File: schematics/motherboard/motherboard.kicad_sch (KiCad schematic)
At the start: 2 parts, among them J1 BATTERY, U1 Raspberry_Pi_Pico

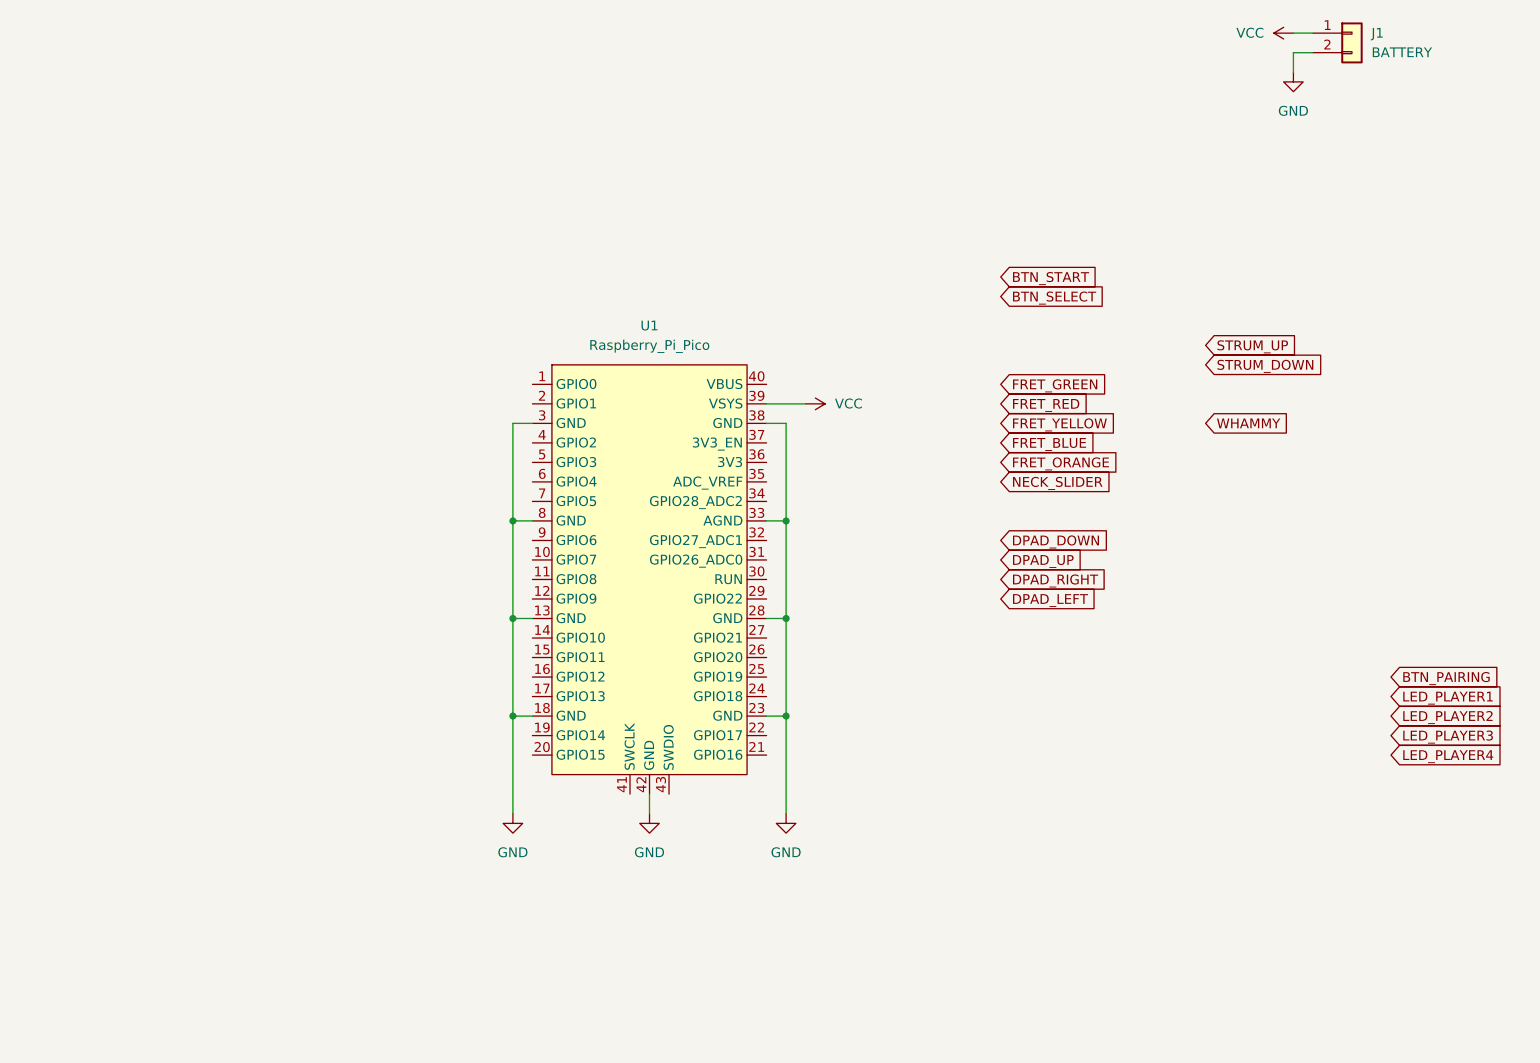
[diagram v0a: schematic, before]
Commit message: Update fret_board, motherboard and strum_bar schematics
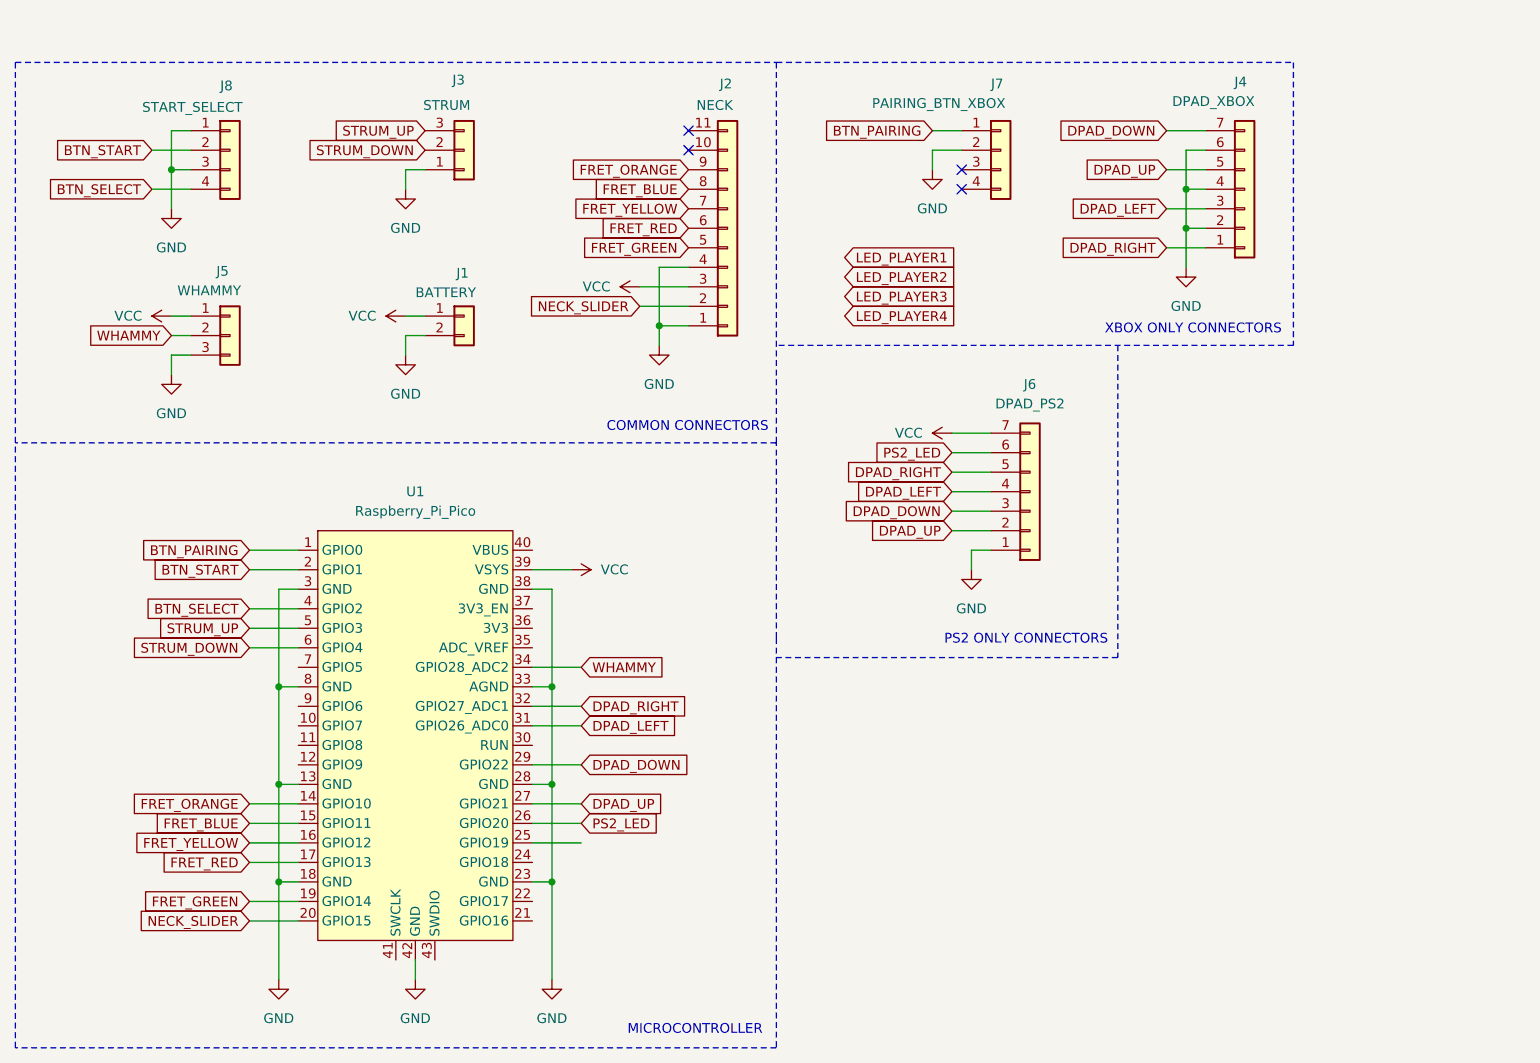
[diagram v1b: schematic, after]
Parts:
- added J2: NECK, Connector_PinHeader_2.00mm:PinHeader_1x11_P2.00mm_Vertical, symbol Connector_Generic:Conn_01x11
- added J3: STRUM, Connector_PinHeader_2.00mm:PinHeader_1x03_P2.00mm_Vertical, symbol Connector_Generic:Conn_01x03
- added J4: DPAD_XBOX, Connector_PinHeader_2.00mm:PinHeader_1x07_P2.00mm_Vertical, symbol Connector_Generic:Conn_01x07
- added J5: WHAMMY, Connector_PinHeader_2.00mm:PinHeader_1x03_P2.00mm_Vertical, symbol Connector_Generic:Conn_01x03
- added J6: DPAD_PS2, Connector_PinHeader_2.00mm:PinHeader_1x07_P2.00mm_Vertical, symbol Connector_Generic:Conn_01x07
- added J7: PAIRING_BTN_XBOX, Connector_PinHeader_2.00mm:PinHeader_1x04_P2.00mm_Vertical, symbol Connector_Generic:Conn_01x04
- added J8: START_SELECT, Connector_PinHeader_2.00mm:PinHeader_1x04_P2.00mm_Vertical, symbol Connector_Generic:Conn_01x04
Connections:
- net BTN_PAIRING: now also U1.1 (GPIO0), J7.1 (Pin_1)
- net BTN_SELECT: now also U1.4 (GPIO2), J8.4 (Pin_4)
- net BTN_START: now also U1.2 (GPIO1), J8.2 (Pin_2)
- net DPAD_DOWN: now also U1.29 (GPIO22), J4.7 (Pin_7), J6.3 (Pin_3)
- net DPAD_LEFT: now also U1.31 (GPIO26_ADC0), J4.3 (Pin_3), J6.4 (Pin_4)
- net DPAD_RIGHT: now also U1.32 (GPIO27_ADC1), J4.1 (Pin_1), J6.5 (Pin_5)
- net DPAD_UP: now also U1.27 (GPIO21), J4.5 (Pin_5), J6.2 (Pin_2)
- net FRET_BLUE: now also U1.15 (GPIO11), J2.8 (Pin_8)
- net FRET_GREEN: now also U1.19 (GPIO14), J2.5 (Pin_5)
- net FRET_ORANGE: now also U1.14 (GPIO10), J2.9 (Pin_9)
- net FRET_RED: now also U1.17 (GPIO13), J2.6 (Pin_6)
- net FRET_YELLOW: now also U1.16 (GPIO12), J2.7 (Pin_7)
- net GND: now also J2.1 (Pin_1), J2.4 (Pin_4), J3.1 (Pin_1), J4.2 (Pin_2), J4.4 (Pin_4), J4.6 (Pin_6), J5.3 (Pin_3), J6.1 (Pin_1), J7.2 (Pin_2), J8.1 (Pin_1), J8.3 (Pin_3)
- net NECK_SLIDER: now also U1.20 (GPIO15), J2.2 (Pin_2)
- net STRUM_DOWN: now also U1.6 (GPIO4), J3.2 (Pin_2)
- net STRUM_UP: now also U1.5 (GPIO3), J3.3 (Pin_3)
- net VCC: now also J2.3 (Pin_3), J5.1 (Pin_1), J6.7 (Pin_7)
- net WHAMMY: now also U1.34 (GPIO28_ADC2), J5.2 (Pin_2)
- net PS2_LED: now reaches U1.26 (GPIO20)
- net PS2_LED: now also J6.6 (Pin_6)
- no-connect marks 0 -> 4
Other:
- note added: "COMMON CONNECTORS"
- note added: "MICROCONTROLLER"
- note added: "PS2 ONLY CONNECTORS"
- note added: "XBOX ONLY CONNECTORS"
- moved on the sheet: J1, U1

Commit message: Add battery sensing circuit and reverse polarity protection diode
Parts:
- added D1: 1N5817, Diode_THT:D_DO-41_SOD81_P7.62mm_Horizontal, symbol Device:D
- added Q1: BC847, Package_TO_SOT_SMD:SOT-23, symbol Transistor_BJT:BC847
- added Q2: IRF5305, Package_TO_SOT_SMD:SOT-23, symbol Simulation_SPICE:PMOS
- added R1, R2, R3: 100k, Resistor_SMD:R_1206_3216Metric, symbol Device:R
- added R4: 330k, Resistor_SMD:R_1206_3216Metric, symbol Device:R
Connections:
- net DPAD_DOWN: now also U1.26 (GPIO20); no longer U1.29 (GPIO22)
- net DPAD_LEFT: now also U1.27 (GPIO21); no longer U1.31 (GPIO26_ADC0)
- net DPAD_RIGHT: now also U1.29 (GPIO22); no longer U1.32 (GPIO27_ADC1)
- net DPAD_UP: now also U1.25 (GPIO19); no longer U1.27 (GPIO21)
- net GND: now also Q1.2 (E), R4.2
- net PS2_LED: now also U1.24 (GPIO18); no longer U1.26 (GPIO20)
- net VCC: now also D1.1 (K), Q2.3 (S), R1.2; no longer J1.1 (Pin_1)
- new net: D1.2 (A), J1.1 (Pin_1)
- new net: Q1.3 (C), Q2.2 (G), R1.1
- new net: Q1.1 (B), R2.1
- new net: Q2.1 (D), R3.1
- new net VBAT_SENSE: R3.2, R4.1, U1.32 (GPIO27_ADC1)
- new net VBAT_SENSE_SWITCH: R2.2, U1.31 (GPIO26_ADC0)
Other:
- note added: "BATTERY SENSE CIRCUIT"

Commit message: Add silkscreen graphics to each schematic
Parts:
- J1: value BATTERY -> BAT
- J8: value START_SELECT -> ST_SEL
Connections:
- net VBAT: now reaches D1.2 (A), J1.1 (Pin_1)
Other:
- moved on the sheet: D1
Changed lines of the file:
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@@
 	(wire
 		(pts
-			(xy 105.41 67.31) (xy 106.68 67.31)
+			(xy 101.6 67.31) (xy 102.87 67.31)
 		)
 		(stroke
@@
 	(wire
 		(pts
-			(xy 114.3 67.31) (xy 115.57 67.31)
+			(xy 110.49 67.31) (xy 115.57 67.31)
 		)
 		(stroke
@@
 		)
 	)
+	(label "VBAT"
+		(at 115.57 67.31 180)
+		(fields_autoplaced yes)
+		(effects
+			(font
+				(size 1.27 1.27)
+			)
+			(justify right bottom)
+		)
+	)
 	(global_label "DPAD_RIGHT"
 		(shape input)
@@
 	(symbol
 		(lib_id "Device:D")
-		(at 110.49 67.31 0)
+		(at 106.68 67.31 0)
 		(unit 1)
 		(exclude_from_sim no)
@@
 		(fields_autoplaced yes)
 		(property "Reference" "D1"
-			(at 110.49 60.96 0)
+			(at 106.68 60.96 0)
 			(effects
 				(font
@@
 		)
 		(property "Value" "1N5817"
-			(at 110.49 63.5 0)
+			(at 106.68 63.5 0)
 			(effects
 				(font
@@
 		)
 		(property "Footprint" "Diode_THT:D_DO-41_SOD81_P7.62mm_Horizontal"
-			(at 110.49 67.31 0)
+			(at 106.68 67.31 0)
 			(effects
 				(font
@@
 		)
 		(property "Datasheet" "https://elektronik-lavpris.dk/p78390/1n5817-schottky-20v-1a-do41/"
-			(at 110.49 67.31 0)
+			(at 106.68 67.31 0)
 			(effects
 				(font
@@
 		)
 		(property "Description" "Diode"
-			(at 110.49 67.31 0)
+			(at 106.68 67.31 0)
 			(effects
 				(font
@@
 		)
 		(property "Sim.Device" "D"
-			(at 110.49 67.31 0)
+			(at 106.68 67.31 0)
 			(effects
 				(font
@@
 		)
 		(property "Sim.Pins" "1=K 2=A"
-			(at 110.49 67.31 0)
+			(at 106.68 67.31 0)
 			(effects
 				(font
@@
 			)
 		)
-		(property "Value" "BATTERY"
-			(at 114.3 64.262 0)
+		(property "Value" "BAT"
+			(at 118.364 64.262 0)
 			(effects
 				(font
@@
 			)
 		)
-		(property "Value" "START_SELECT"
-			(at 78.74 40.132 0)
+		(property "Value" "ST_SEL"
+			(at 84.836 39.878 0)
 			(effects
 				(font
@@
 	(symbol
 		(lib_id "power:VCC")
-		(at 105.41 67.31 90)
+		(at 101.6 67.31 90)
 		(unit 1)
 		(exclude_from_sim no)
@@
 		(fields_autoplaced yes)
 		(property "Reference" "#PWR05"
-			(at 109.22 67.31 0)
+			(at 105.41 67.31 0)
 			(effects
 				(font
@@
 		)
 		(property "Value" "VCC"
-			(at 101.6 67.3099 90)
+			(at 97.79 67.3099 90)
 			(effects
 				(font
@@
 		)
 		(property "Footprint" ""
-			(at 105.41 67.31 0)
+			(at 101.6 67.31 0)
 			(effects
 				(font
@@
 		)
 		(property "Datasheet" ""
-			(at 105.41 67.31 0)
+			(at 101.6 67.31 0)
 			(effects
 				(font
@@
 		)
 		(property "Description" "Power symbol creates a global label with name \"VCC\""
-			(at 105.41 67.31 0)
+			(at 101.6 67.31 0)
 			(effects
 				(font

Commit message: Update Q2 to proper footprint and fix wrong R3/R4 silkscreen
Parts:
- removed Q2: IRF5305, Package_TO_SOT_SMD:SOT-23, symbol Simulation_SPICE:PMOS
- added Q2: BSS84, Package_TO_SOT_SMD:SOT-23, symbol Transistor_FET:BSS84
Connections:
- net VCC: now also Q2.2 (S)
- net at Q1.3 (C), R1.1: now also Q2.1 (G)
- net at R3.1: now also Q2.3 (D)
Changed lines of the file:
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@@
 (kicad_sch
-	(version 20231120)
+	(version 20250114)
 	(generator "eeschema")
-	(generator_version "8.0")
+	(generator_version "9.0")
 	(paper "A4")
+	(text "BATTERY SENSE CIRCUIT"
+		(exclude_from_sim no)
+		(at 234.95 161.036 0)
+		(effects
+			(font
+				(size 1.27 1.27)
+			)
+			(justify right)
+		)
+	)
+	(text "COMMON CONNECTORS"
+		(exclude_from_sim no)
+		(at 160.274 81.788 0)
+		(effects
+			(font
+				(size 1.27 1.27)
+			)
+			(justify right)
+		)
+	)
+	(text "MICROCONTROLLER"
+		(exclude_from_sim no)
+		(at 159.512 160.274 0)
+		(effects
+			(font
+				(size 1.27 1.27)
+			)
+			(justify right)
+		)
+	)
+	(text "XBOX ONLY CONNECTORS"
+		(exclude_from_sim no)
+		(at 227.076 69.088 0)
+		(effects
+			(font
+				(size 1.27 1.27)
+			)
+			(justify right)
+		)
+	)
+	(text "PS2 ONLY CONNECTORS"
+		(exclude_from_sim no)
+		(at 204.47 109.474 0)
+		(effects
+			(font
+				(size 1.27 1.27)
+			)
+			(justify right)
+		)
+	)
 	(junction
 		(at 132.08 115.57)
@@
 		)
 	)
-	(text "BATTERY SENSE CIRCUIT"
-		(exclude_from_sim no)
-		(at 234.95 161.036 0)
-		(effects
-			(font
-				(size 1.27 1.27)
-			)
-			(justify right)
-		)
-	)
-	(text "COMMON CONNECTORS"
-		(exclude_from_sim no)
-		(at 160.274 81.788 0)
-		(effects
-			(font
-				(size 1.27 1.27)
-			)
-			(justify right)
-		)
-	)
-	(text "MICROCONTROLLER"
-		(exclude_from_sim no)
-		(at 159.512 160.274 0)
-		(effects
-			(font
-				(size 1.27 1.27)
-			)
-			(justify right)
-		)
-	)
-	(text "XBOX ONLY CONNECTORS"
-		(exclude_from_sim no)
-		(at 227.076 69.088 0)
-		(effects
-			(font
-				(size 1.27 1.27)
-			)
-			(justify right)
-		)
-	)
-	(text "PS2 ONLY CONNECTORS"
-		(exclude_from_sim no)
-		(at 204.47 109.474 0)
-		(effects
-			(font
-				(size 1.27 1.27)
-			)
-			(justify right)
-		)
-	)
 	(label "VBAT"
 		(at 115.57 67.31 180)
-		(fields_autoplaced yes)
 		(effects
 			(font
@@
 	)
 	(symbol
+		(lib_id "Transistor_FET:BSS84")
+		(at 201.93 124.46 270)
+		(mirror x)
+		(unit 1)
+		(exclude_from_sim no)
+		(in_bom yes)
+		(on_board yes)
+		(dnp no)
+		(fields_autoplaced yes)
+		(property "Reference" "Q2"
+			(at 201.93 115.57 90)
+			(effects
+				(font
+					(size 1.27 1.27)
+				)
+			)
+		)
+		(property "Value" "BSS84"
+			(at 201.93 118.11 90)
+			(effects
+				(font
+					(size 1.27 1.27)
+				)
+			)
+		)
+		(property "Footprint" "Package_TO_SOT_SMD:SOT-23"
+			(at 200.025 119.38 0)
+			(effects
+				(font
+					(size 1.27 1.27)
+					(italic yes)
+				)
+				(justify left)
+				(hide yes)
+			)
+		)
+		(property "Datasheet" "http://assets.nexperia.com/documents/data-sheet/BSS84.pdf"
+			(at 198.12 119.38 0)
+			(effects
+				(font
+					(size 1.27 1.27)
+				)
+				(justify left)
+				(hide yes)
+			)
+		)
+		(property "Description" "-0.13A Id, -50V Vds, P-Channel MOSFET, SOT-23"
+			(at 201.93 124.46 0)
+			(effects
+				(font
+					(size 1.27 1.27)
+				)
+				(hide yes)
+			)
+		)
+		(pin "2"
+		)
+		(pin "1"
+		)
+		(pin "3"
+		)
+		(instances
+			(project ""
+				(path "/b0ae2863-e73e-4a7c-8497-4366602b6808"
+					(reference "Q2")
+					(unit 1)
+				)
+			)
+		)
+	)
+	(symbol
 		(lib_id "power:GND")
 		(at 146.05 71.12 0)
@@
 	)
 	(symbol
-		(lib_id "Simulation_SPICE:PMOS")
-		(at 201.93 124.46 270)
-		(mirror x)
-		(unit 1)
-		(exclude_from_sim no)
-		(in_bom yes)
-		(on_board yes)
-		(dnp no)
-		(property "Reference" "Q2"
-			(at 201.93 115.57 90)
-			(effects
-				(font
-					(size 1.27 1.27)
-				)
-			)
-		)
-		(property "Value" "IRF5305"
-			(at 201.93 118.11 90)
-			(effects
-				(font
-					(size 1.27 1.27)
-				)
-			)
-		)
-		(property "Footprint" "Package_TO_SOT_SMD:SOT-23"
-			(at 204.47 119.38 0)
-			(effects
-				(font
-					(size 1.27 1.27)
-				)
-				(hide yes)
-			)
-		)
-		(property "Datasheet" "https://ngspice.sourceforge.io/docs/ngspice-html-manual/manual.xhtml#cha_MOSFETs"
-			(at 189.23 124.46 0)
-			(effects
-				(font
-					(size 1.27 1.27)
-				)
-				(hide yes)
-			)
-		)
-		(property "Description" "P-MOSFET transistor, drain/source/gate"
-			(at 201.93 124.46 0)
-			(effects
-				(font
-					(size 1.27 1.27)
-				)
-				(hide yes)
-			)
-		)
-		(property "Sim.Device" "PMOS"
-			(at 184.785 124.46 0)
-			(effects
-				(font
-					(size 1.27 1.27)
-				)
-				(hide yes)
-			)
-		)
-		(property "Sim.Type" "VDMOS"
-			(at 182.88 124.46 0)
-			(effects
-				(font
-					(size 1.27 1.27)
-				)
-				(hide yes)
-			)
-		)
-		(property "Sim.Pins" "1=D 2=G 3=S"
-			(at 186.69 124.46 0)
-			(effects
-				(font
-					(size 1.27 1.27)
-				)
-				(hide yes)
-			)
-		)
-		(pin "1"
-		)
-		(pin "2"
-		)
-		(pin "3"
-		)
-		(instances
-			(project ""
-				(path "/b0ae2863-e73e-4a7c-8497-4366602b6808"
-					(reference "Q2")
-					(unit 1)
-				)
-			)
-		)
-	)
-	(symbol
 		(lib_id "Connector_Generic:Conn_01x11")
 		(at 154.94 55.88 0)
@@
 		)
 	)
+	(embedded_fonts no)
 )
